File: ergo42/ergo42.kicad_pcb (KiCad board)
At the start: 2 copper layers, 135.9 x 98.4 mm, 68 parts, among them J1 5PIN, SW1 SW_PUSH, SW10 SW_PUSH, SW11 SW_PUSH, SW12 SW_PUSH, SW13 SW_PUSH, SW14 SW_PUSH, SW15 SW_PUSH, SW16 SW_PUSH, SW17 SW_PUSH, SW18 SW_PUSH, SW19 SW_PUSH, SW2 SW_PUSH, SW20 SW_PUSH, SW21 SW_PUSH, SW22 SW_PUSH, SW23 SW_PUSH, SW24 SW_PUSH, SW25 SW_PUSH, SW26 SW_PUSH, SW27 SW_PUSH, SW28 SW_PUSH, SW29 SW_Push, SW3 SW_PUSH, SW4 SW_PUSH, SW5 SW_PUSH, SW6 SW_PUSH, SW7 SW_PUSH, SW8 SW_PUSH, SW9 SW_PUSH, U1 HOLE, U2 HOLE, U3 ProMicro, U4 HOLE, U5 HOLE, U7 HOLE

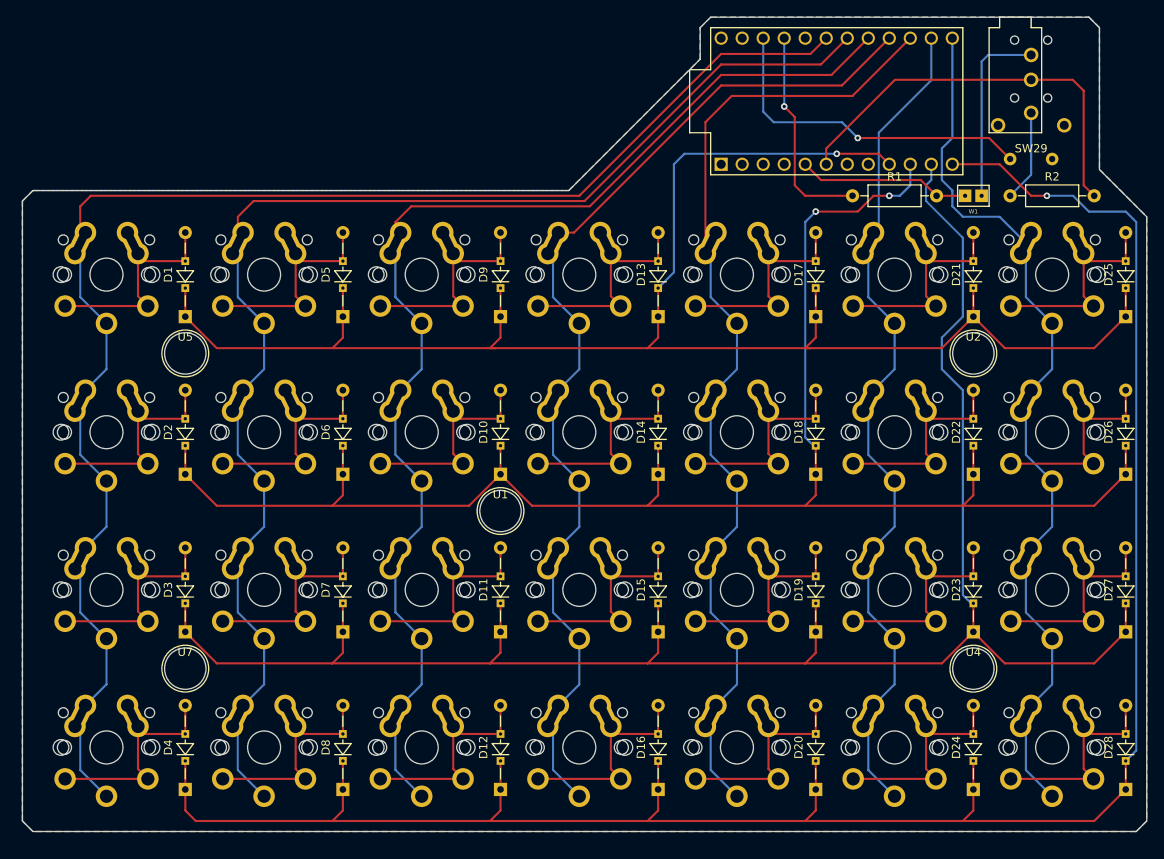
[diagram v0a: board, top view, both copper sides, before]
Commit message: Make meishi switch
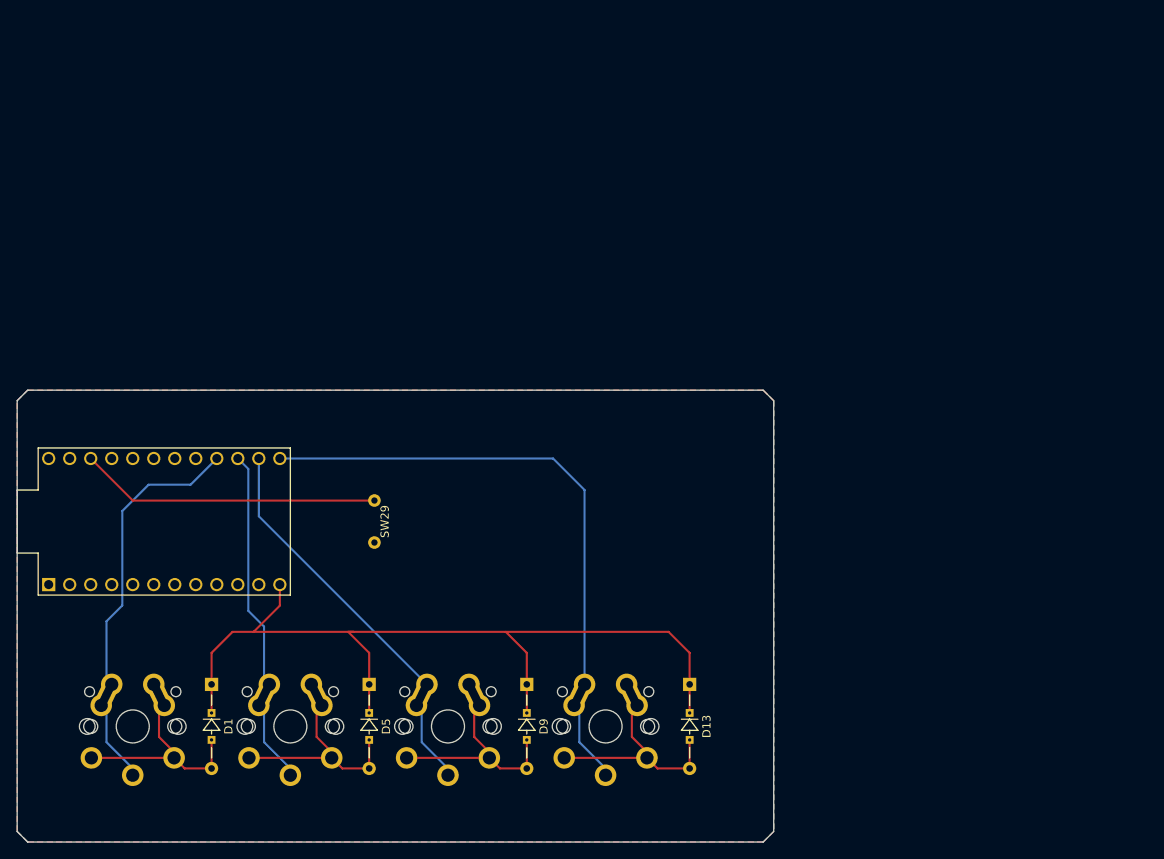
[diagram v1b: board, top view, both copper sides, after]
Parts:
- removed D10, D11, D12, D14, D15, D16, D17, D18, D19, D2, D20, D21, D22, D23, D24, D25, D26, D27, D28, D3, D4, D6, D7, D8: D, library:Diode_SMD_THT
- removed G***: LOGO, library:ergo42_logo
- removed J1: 5PIN, library:trrs_jack
- removed R1, R2: R, Resistors_THT:R_Axial_DIN0207_L6.3mm_D2.5mm_P10.16mm_Horizontal
- removed SW10, SW11, SW12, SW14, SW15, SW16, SW17, SW18, SW19, SW2, SW20, SW21, SW22, SW23, SW24, SW25, SW26, SW27, SW28, SW3, SW4, SW6, SW7, SW8: SW_PUSH, library:key_switch
- removed U1, U2, U4, U5, U7: HOLE, library:hole
- removed W1: jumper_smd, library:jumper_smd_2dub
- moved U3 95.8 mm to (91.4, 103.5)
- moved SW29 90.7 mm to (116.8, 103.5), turned to 270 degrees
- moved SW1 54.7 mm to (87.6, 128.3)
- moved SW13 54.7 mm to (144.8, 128.3)
- moved SW5 54.7 mm to (106.7, 128.3)
- moved SW9 54.7 mm to (125.7, 128.3)
- moved D13 44.6 mm to (154.9, 123.2), turned to 270 degrees
- moved D1 44.6 mm to (97.2, 123.2), turned to 270 degrees
- moved D5 44.6 mm to (116.2, 123.2), turned to 270 degrees
- moved D9 44.6 mm to (135.3, 123.2), turned to 270 degrees
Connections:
- U3 pad 10: /row1 -> Net-(U3-Pad10)
- U3 pad 11: /row2 -> Net-(U3-Pad11)
- U3 pad 12: /row3 -> /row0
- U3 pad 13: /col6 -> /col3
- U3 pad 14: /col5 -> /col2
- U3 pad 15: /col4 -> /col1
- U3 pad 16: /col3 -> /col0
- U3 pad 17: /col2 -> Net-(U3-Pad17)
- U3 pad 18: /col1 -> Net-(U3-Pad18)
- U3 pad 19: /col0 -> Net-(U3-Pad19)
- U3 pad 5: /scl -> Net-(U3-Pad5)
- U3 pad 6: /sda/uart -> Net-(U3-Pad6)
- U3 pad 9: /row0 -> Net-(U3-Pad9)
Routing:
- net /row3: track 255.5 -> 0.00 mm, vias 1 -> 0
- net /row2: track 219.8 -> 0.00 mm
- net /row1: track 206.3 -> 0.00 mm, vias 2 -> 0
- net /col0: track 178.8 -> 48.1 mm
- net /col4: track 122.0 -> 0.00 mm
- net /col1: track 161.5 -> 40.9 mm
- net /col6: track 107.8 -> 0.00 mm
- net /col5: track 103.6 -> 0.00 mm
- net /row0: track 205.6 -> 103.8 mm, vias 1 -> 0
- net /col2: track 144.6 -> 48.2 mm
- net /col3: track 126.9 -> 74.3 mm
- net /sda/uart: track 50.2 -> 0.00 mm
- net VCC: track 36.9 -> 0.00 mm, vias 1 -> 0
- net Net-(D6-Pad2): track 27.1 -> 0.00 mm
- net Net-(D10-Pad2): track 26.4 -> 0.00 mm
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- added copper zone on F.Cu, net GND
- removed copper zone on F.Cu, net VCC
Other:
- board size 135.9 x 98.4 mm -> 91.4 x 54.6 mm
- board text removed: "Ergo42 by Biacco42"

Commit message: Implement
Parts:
- added G***: LOGO, library:biacco42, F.Cu at (142.2, 103.5)
- added G***: LOGO, library:tanoshii_life, B.Cu at (142.9, 106.7)
- moved U3 6.38 mm to (97.8, 104.1)
- moved SW29 4.49 mm to (121.3, 104.1)
- moved SW1 1.80 mm to (88.9, 127.0)
- moved SW13 1.80 mm to (146.1, 127.0)
- moved D9 1.80 mm to (136.5, 121.9)
- moved SW5 1.80 mm to (108.0, 127.0)
- moved SW9 1.80 mm to (127.0, 127.0)
- moved D1 1.80 mm to (98.4, 121.9)
- moved D5 1.80 mm to (117.5, 121.9)
- moved D13 1.42 mm to (155.6, 121.9)
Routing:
- net /col3: track 74.3 -> 65.5 mm
- net /row0: track 103.8 -> 98.4 mm
- net /col2: track 48.2 -> 43.7 mm
- net /col1: track 40.9 -> 38.5 mm
- net /rst: track 36.4 -> 34.5 mm
- net /col0: track 48.1 -> 49.0 mm
- net Net-(D9-Pad2): track 26.9 -> 27.6 mm
- net Net-(D5-Pad2): track 26.9 -> 27.6 mm
- net Net-(D1-Pad2): track 26.9 -> 27.6 mm
